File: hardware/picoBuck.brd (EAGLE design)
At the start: 36.2 x 29.8 mm, 37 parts, among them U1 AL8805WS, U2 AL8805WS, U3 AL8805WS

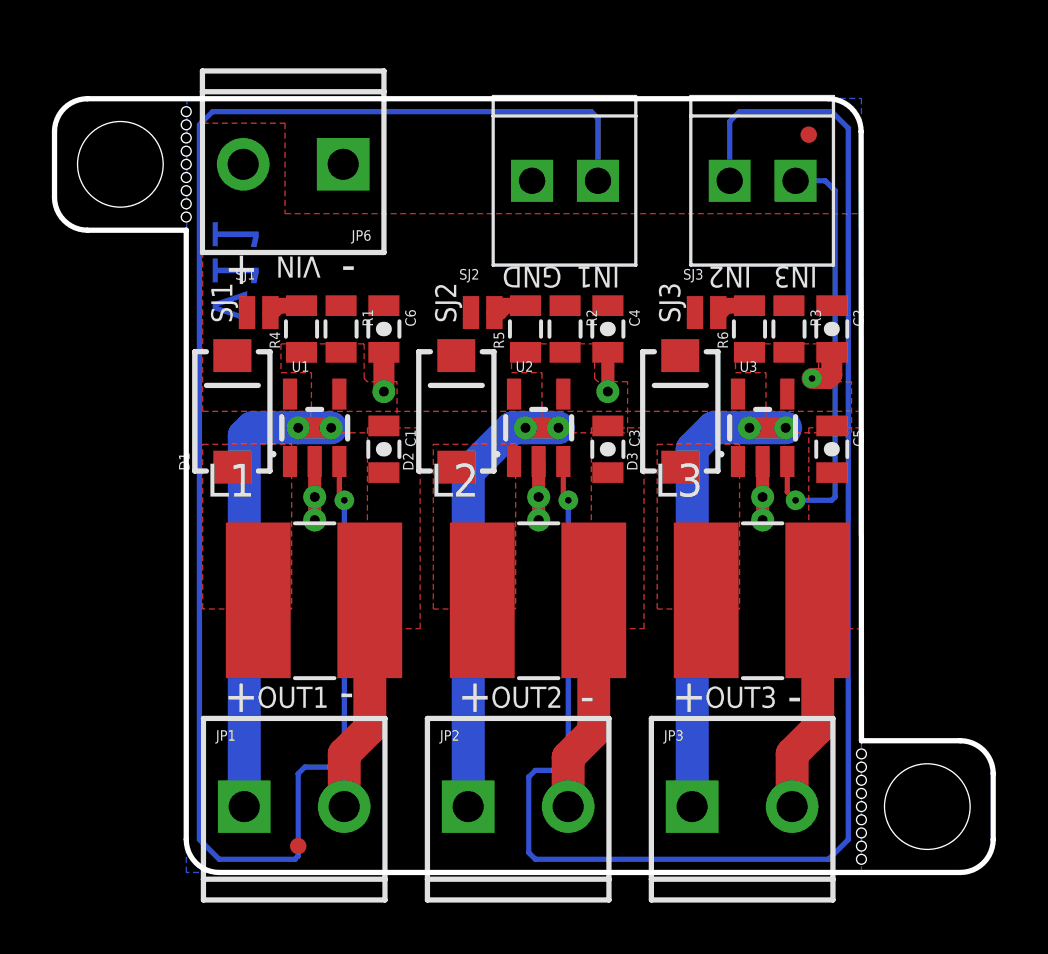
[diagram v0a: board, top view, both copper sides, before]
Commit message: Added some silk to back of board
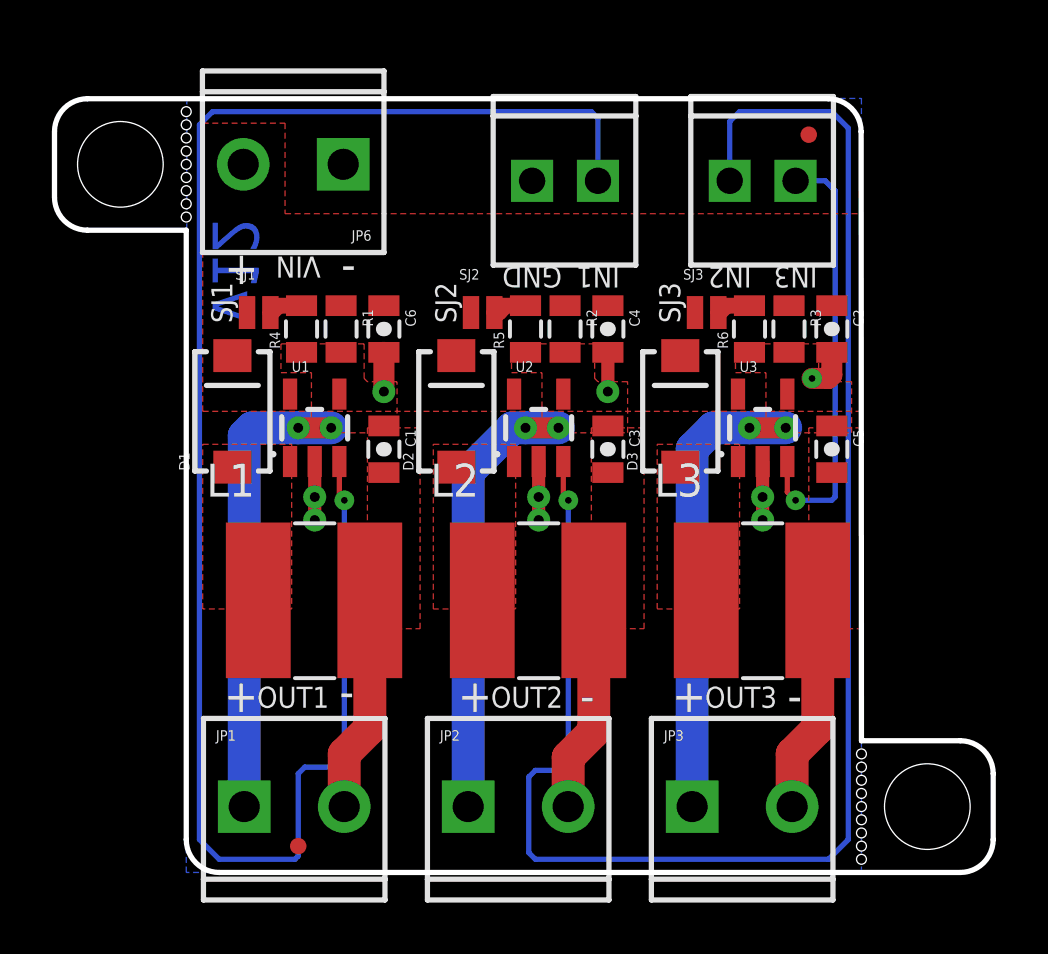
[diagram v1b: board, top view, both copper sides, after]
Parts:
- moved LOGO2 0.81 mm to (22.6, 3.94)
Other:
- board text added: "6-36V 3-chan 330/660mA LED Driver"
- board text added: "v12"
- board text removed: "v11"
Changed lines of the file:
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@@
 <text x="20.955" y="23.368" size="0.8128" layer="21" font="vector" ratio="15" rot="SR180" align="bottom-center">IN2</text>
 <text x="23.495" y="23.368" size="0.8128" layer="21" font="vector" ratio="15" rot="SR180" align="bottom-center">IN3</text>
-<text x="20.8153" y="9.8552" size="1.778" layer="22" font="vector" ratio="15" rot="MR0">picoBuck</text>
-<wire x1="0.635" y1="9.525" x2="4.318" y2="9.525" width="0.3048" layer="22" style="shortdash"/>
-<wire x1="4.318" y1="9.525" x2="6.223" y2="12.7" width="0.3048" layer="22" style="shortdash"/>
-<wire x1="6.223" y1="12.7" x2="21.59" y2="12.7" width="0.3048" layer="22" style="shortdash"/>
-<wire x1="21.59" y1="12.7" x2="23.495" y2="9.525" width="0.3048" layer="22" style="shortdash"/>
-<wire x1="23.495" y1="9.525" x2="26.035" y2="9.525" width="0.3048" layer="22" style="shortdash"/>
-<text x="2.794" y="25.273" size="1.778" layer="16" font="vector" ratio="15" rot="MR270">v11</text>
+<text x="13.3223" y="10.9982" size="1.778" layer="22" font="vector" ratio="15" rot="MR0" align="center">picoBuck</text>
+<text x="2.794" y="25.273" size="1.778" layer="16" font="vector" ratio="15" rot="MR270">v12</text>
 <text x="13.335" y="23.368" size="0.8128" layer="21" font="vector" ratio="15" rot="SR180" align="bottom-center">GND</text>
 <wire x1="31.115" y1="3.81" x2="31.115" y2="1.27" width="0.2032" layer="20"/>
@@
 <text x="10.414" y="21.971" size="0.8128" layer="21" font="vector" ratio="15" rot="R90" align="bottom-center">SJ2</text>
 <text x="19.05" y="21.971" size="0.8128" layer="21" font="vector" ratio="15" rot="R90" align="bottom-center">SJ3</text>
+<text x="13.97" y="22.225" size="1.27" layer="22" font="vector" ratio="15" rot="MR0" align="center">6-36V 3-chan
+330/660mA
+LED Driver</text>
+<dimension x1="-2.54" y1="27.305" x2="28.575" y2="2.54" x3="13.0175" y3="34.29" textsize="1.778" textratio="15" layer="47" dtype="horizontal" unit="inch" precision="4"/>
+<dimension x1="-1.27" y1="2.54" x2="-2.54" y2="27.305" x3="-10.16" y3="14.9225" textsize="1.778" textratio="15" layer="47" dtype="vertical" unit="inch" precision="4"/>
 </plain>
 <attributes>
@@
 </element>
 <element name="LOGO1" library="SparkFun-Aesthetics" package="OSHW-LOGO-S" value="OSHW-LOGOS" x="10.16" y="27.305" rot="MR0"/>
-<element name="LOGO2" library="SparkFun-Aesthetics" package="SFE-NEW-WEBLOGO" value="LOGO-SFENEW" x="23.241" y="3.429" rot="MR0"/>
+<element name="LOGO2" library="SparkFun-Aesthetics" package="SFE-NEW-WEBLOGO" value="LOGO-SFENEW" x="22.606" y="3.937" rot="MR0"/>
 <element name="FRAME1" library="SparkFun-Aesthetics" package="CREATIVE_COMMONS" value="FRAME-LETTER" x="11.43" y="-31.75"/>
 <element name="JP4" library="SparkFun-Connectors" package="1X02_2.54_SCREWTERM" value="M022.54MM_SCREWTERM" x="20.955" y="26.67"/>
@@
 </board>
 </drawing>
+<compatibility>
+<note version="6.3" minversion="6.2.2" severity="warning">
+Since Version 6.2.2 text objects can contain more than one line,
+which will not be processed correctly with this version.
+</note>
+</compatibility>
 </eagle>

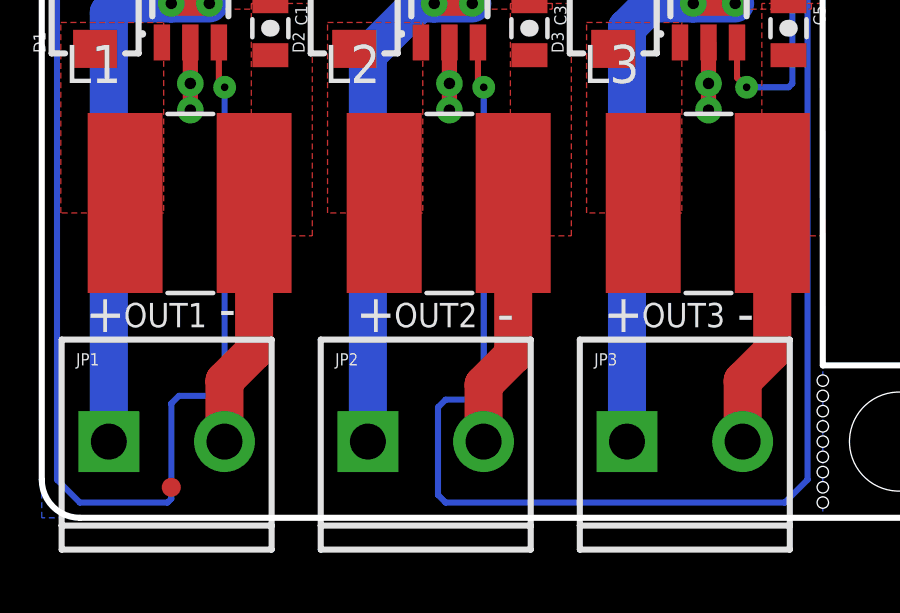
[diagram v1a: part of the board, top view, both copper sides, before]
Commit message: Center text on center screw term, add gnd symbols to JP4/5
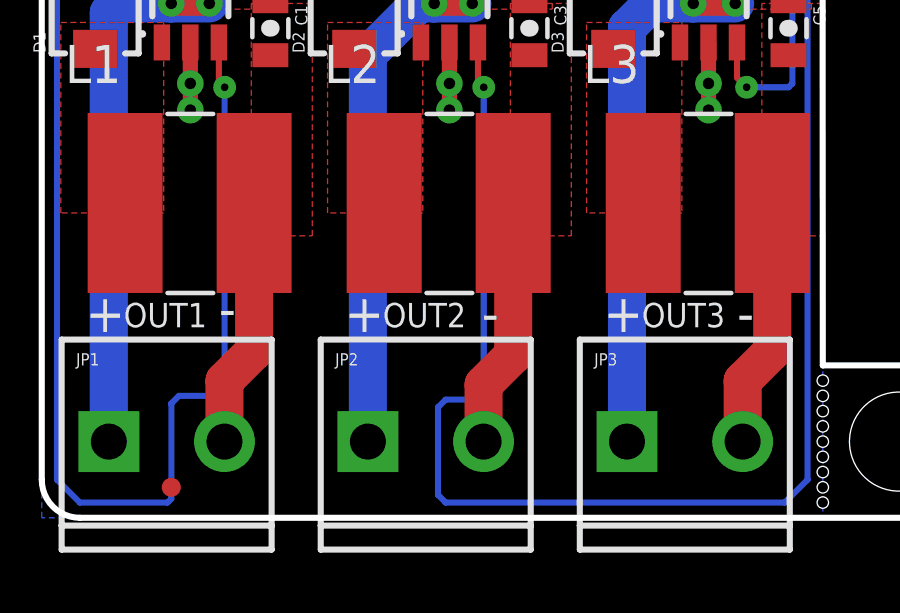
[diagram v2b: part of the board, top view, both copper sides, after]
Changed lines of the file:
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@@
 <setting verticaltext="up"/>
 </settings>
-<grid distance="0.05" unitdist="inch" unit="inch" style="lines" multiple="1" display="yes" altdistance="0.005" altunitdist="inch" altunit="inch"/>
+<grid distance="0.05" unitdist="inch" unit="inch" style="lines" multiple="1" display="no" altdistance="0.005" altunitdist="inch" altunit="inch"/>
 <layers>
 <layer number="1" name="Top" color="4" fill="1" visible="yes" active="yes"/>
@@
 <wire x1="-3.81" y1="29.835" x2="-5.08" y2="28.565" width="0.2032" layer="20" curve="90"/>
 <text x="2.7305" y="6.35" size="0.8128" layer="21" font="vector" ratio="15">OUT1</text>
-<text x="11.7475" y="6.35" size="0.8128" layer="21" font="vector" ratio="15">OUT2</text>
+<text x="11.3665" y="6.35" size="0.8128" layer="21" font="vector" ratio="15">OUT2</text>
 <text x="20.0025" y="6.35" size="0.8128" layer="21" font="vector" ratio="15">OUT3</text>
 <text x="1.4605" y="6.19125" size="1.27" layer="21" font="vector" ratio="15">+</text>
 <text x="5.9055" y="6.35" size="1.27" layer="21" font="vector" ratio="15">-</text>
-<text x="10.4775" y="6.19125" size="1.27" layer="21" font="vector" ratio="15">+</text>
+<text x="10.0965" y="6.19125" size="1.27" layer="21" font="vector" ratio="15">+</text>
 <text x="18.7325" y="6.19125" size="1.27" layer="21" font="vector" ratio="15">+</text>
-<text x="15.1765" y="6.19125" size="1.27" layer="21" font="vector" ratio="15">-</text>
+<text x="14.6685" y="6.19125" size="1.27" layer="21" font="vector" ratio="15">-</text>
 <text x="23.1775" y="6.19125" size="1.27" layer="21" font="vector" ratio="15">-</text>
 <text x="4.318" y="23.749" size="0.8128" layer="21" font="vector" ratio="15" rot="SR180" align="bottom-center">VIN</text>

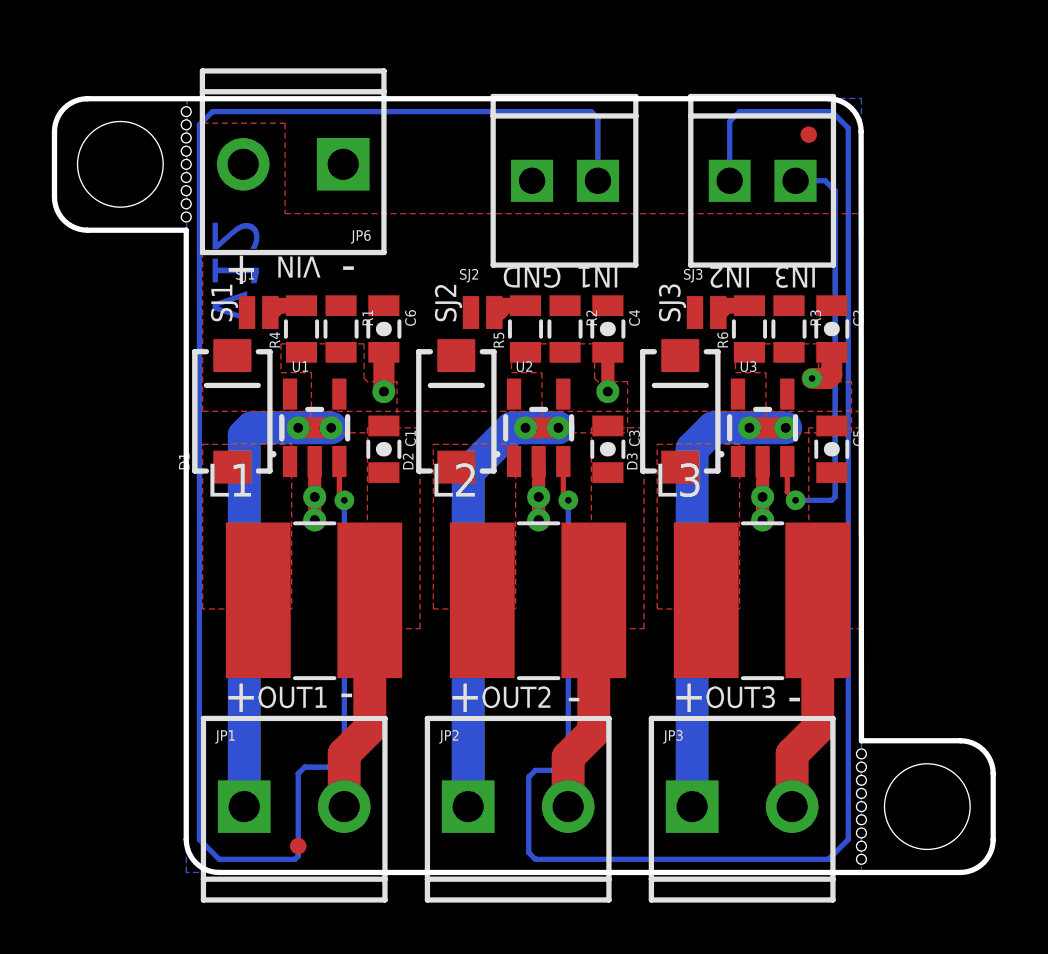
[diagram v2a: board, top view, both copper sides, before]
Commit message: Adjusted upper dim line for panelization
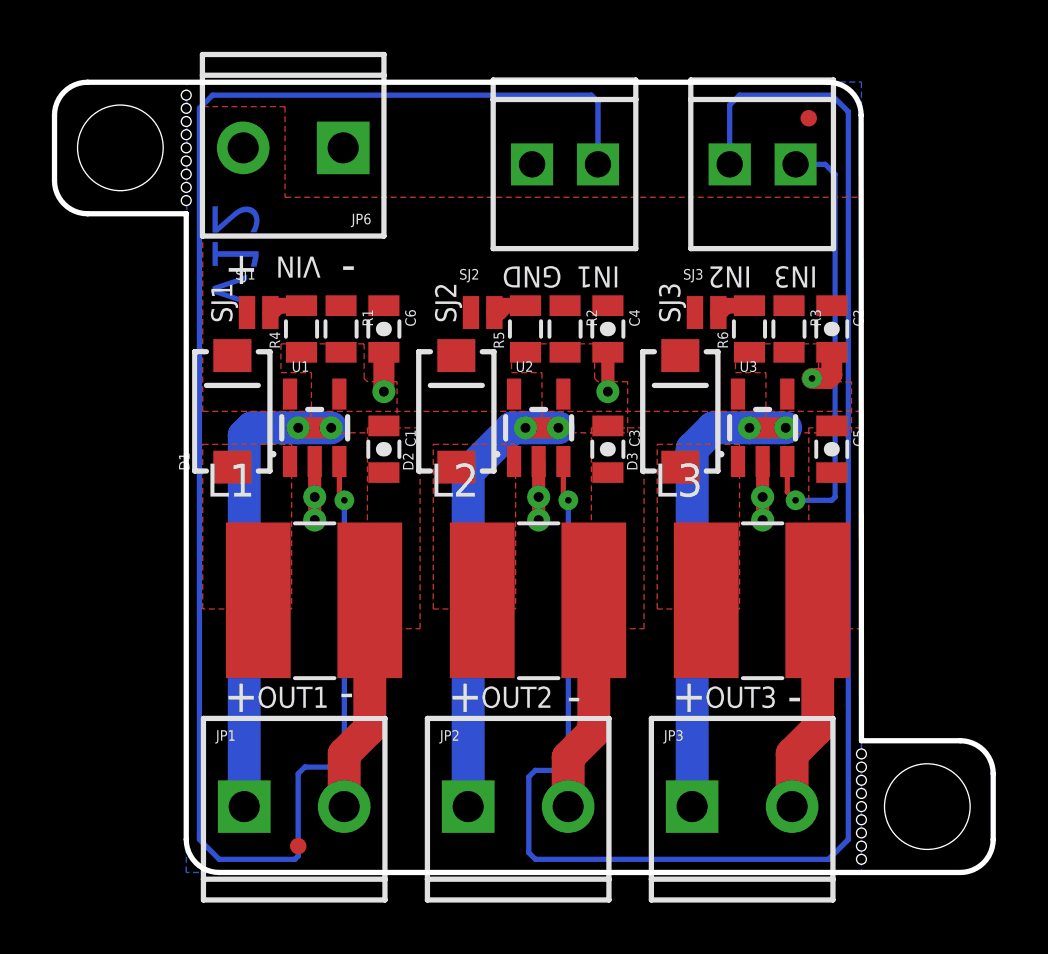
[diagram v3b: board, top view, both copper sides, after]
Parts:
- moved JP6 0.64 mm to (5.87, 27.9)
- moved LOGO1 0.64 mm to (10.2, 27.9)
- moved STANDOFF1 0.64 mm to (-2.54, 27.9)
- moved FID2 0.63 mm to (24.0, 29.1)
- moved JP4 0.63 mm to (21.0, 27.3)
- moved JP5 0.63 mm to (13.3, 27.3)
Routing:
- net CTRL_CH2: track 63.8 -> 64.5 mm
- net CTRL_CH1: track 66.6 -> 67.2 mm
- net CTRL_CH3: track 16.7 -> 17.3 mm
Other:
- board size 36.2 x 29.8 mm -> 36.2 x 30.5 mm
